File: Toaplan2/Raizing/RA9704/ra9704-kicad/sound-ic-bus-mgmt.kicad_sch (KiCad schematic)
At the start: 5 parts, among them U715 PCM_EXP1 (GAL16V8), U716 PCM_EX23 (GAL16V8), U76 A101B

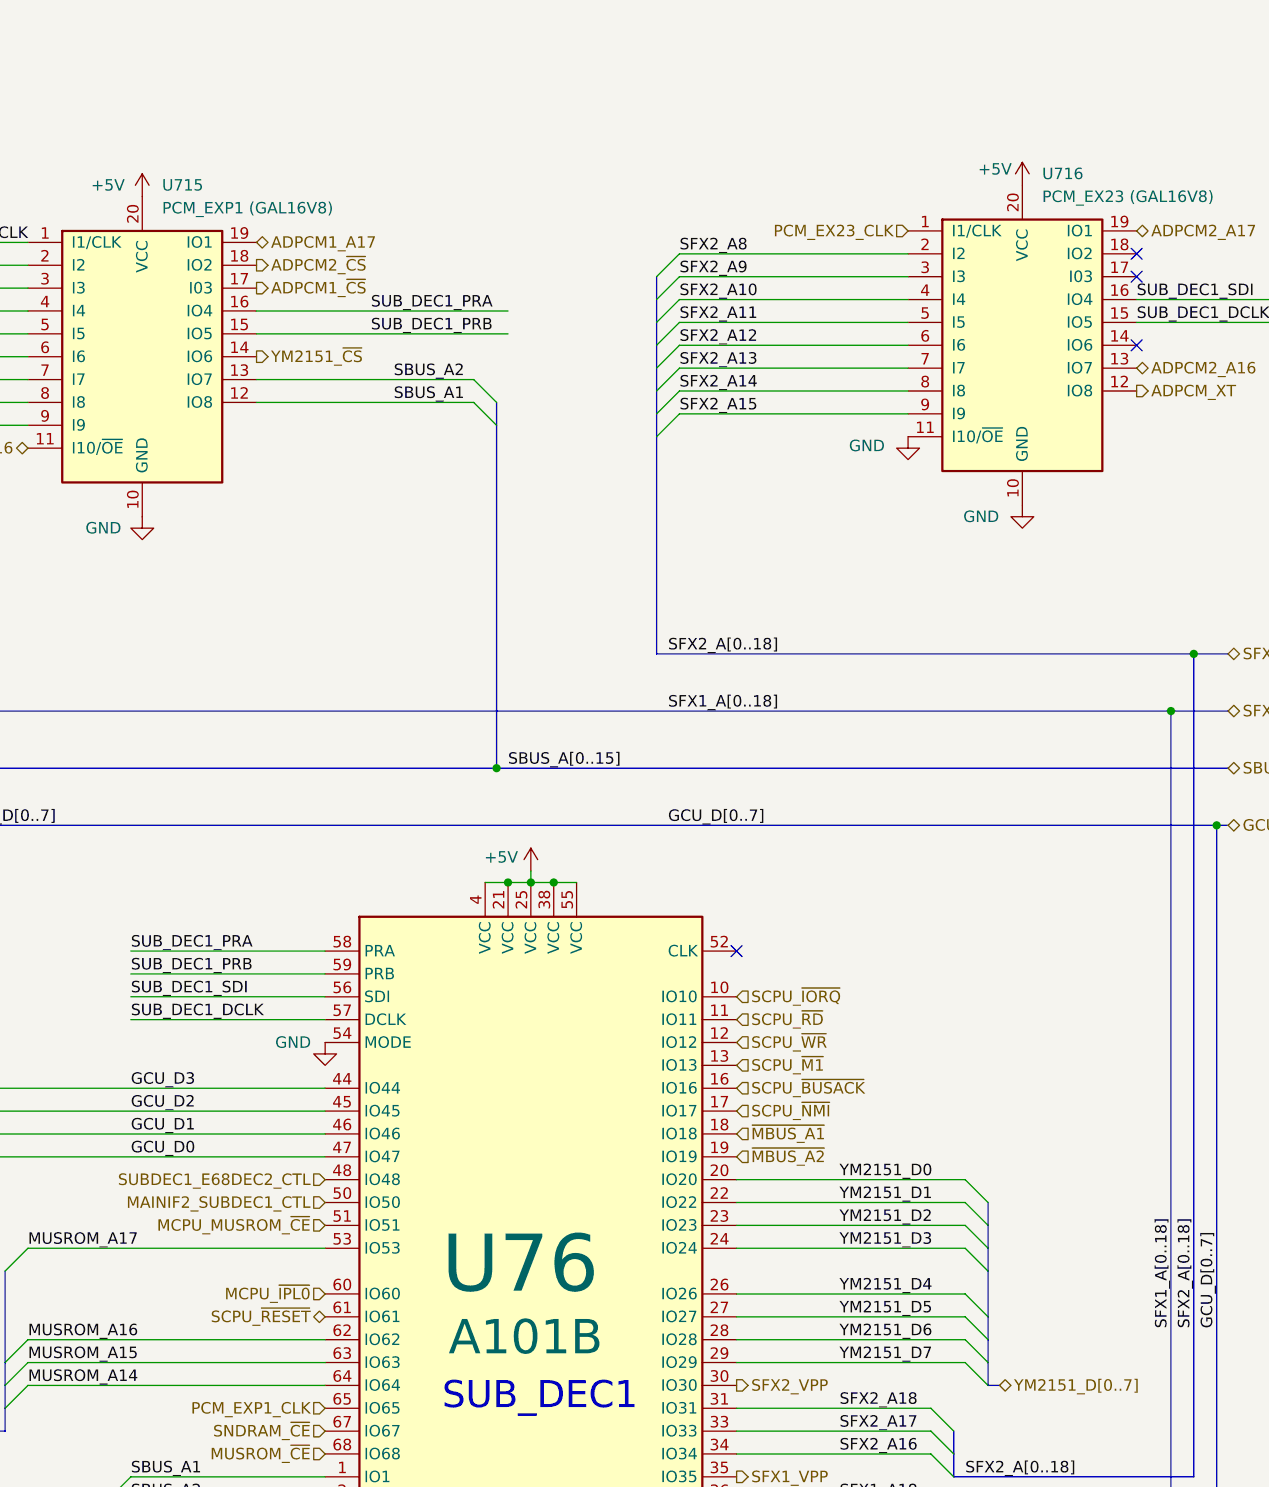
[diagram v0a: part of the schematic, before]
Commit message: fix(ra9704): Add Os as a proxy for 0s in all reference designators
RA9704 has reference designators such that each number has a preceding zero (e.g. RA076, U074, etc.). This causes a bug in KiCAD.

This is 'fixed' by using the 'O' (the letter 'Oh') character instead.

For more info, see the following issue on the KiCAD Gitlab repo

https://gitlab.com/kicad/code/kicad/-/issues/19229
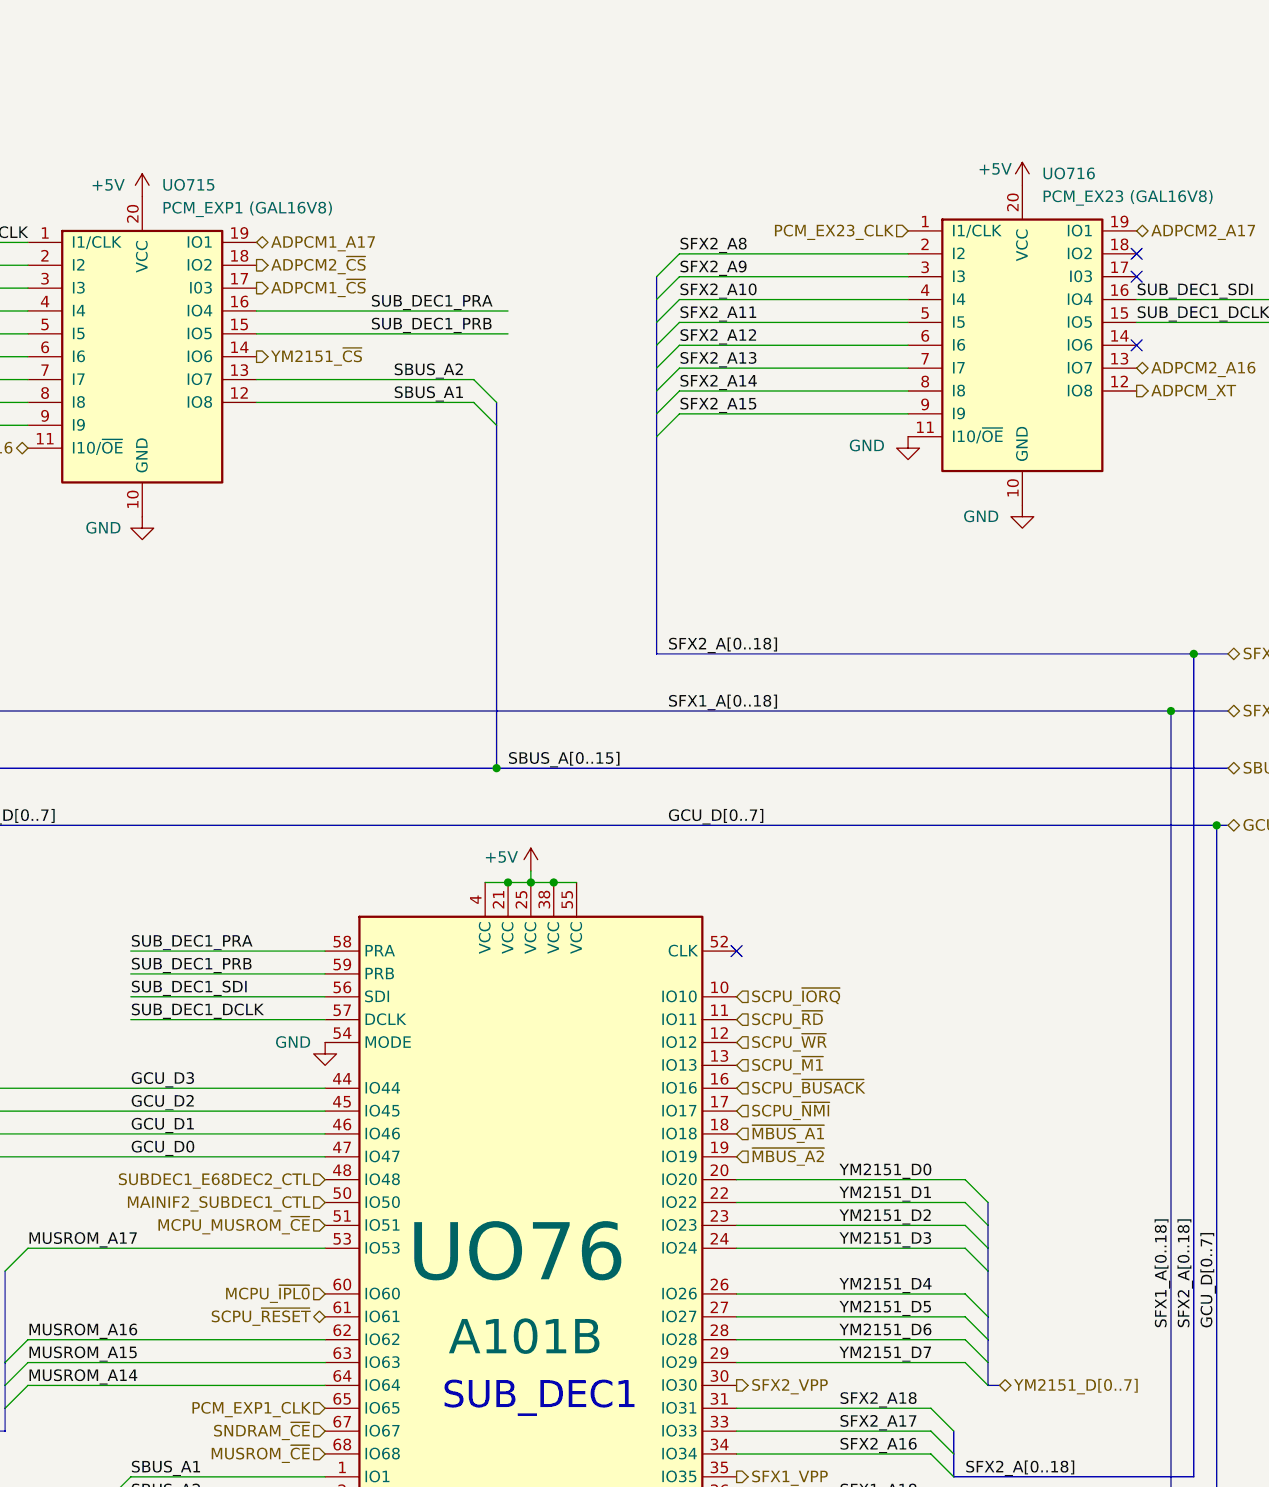
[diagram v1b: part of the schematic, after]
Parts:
- renumbered U715 to UO715, U716 to UO716, U76 to UO76
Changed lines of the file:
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@@
 		(dnp no)
 		(fields_autoplaced yes)
-		(property "Reference" "U716"
+		(property "Reference" "UO716"
 			(at 164.7541 53.34 0)
 			(effects
@@
 			(project "ra9704"
 				(path "/24d3b4cf-2360-45fc-8c40-cedc8afdf9e1/2c170486-a7cf-4da9-9098-f4bf25efe1be"
-					(reference "U716")
+					(reference "UO716")
 					(unit 1)
 				)
@@
 		(on_board yes)
 		(dnp no)
-		(property "Reference" "U76"
-			(at 98.044 174.498 0)
+		(property "Reference" "UO76"
+			(at 94.234 173.228 0)
 			(effects
 				(font
@@
 			(project "ra9704"
 				(path "/24d3b4cf-2360-45fc-8c40-cedc8afdf9e1/2c170486-a7cf-4da9-9098-f4bf25efe1be"
-					(reference "U76")
+					(reference "UO76")
 					(unit 1)
 				)
@@
 		(dnp no)
 		(fields_autoplaced yes)
-		(property "Reference" "U715"
+		(property "Reference" "UO715"
 			(at 66.9641 54.61 0)
 			(effects
@@
 			(project "ra9704"
 				(path "/24d3b4cf-2360-45fc-8c40-cedc8afdf9e1/2c170486-a7cf-4da9-9098-f4bf25efe1be"
-					(reference "U715")
+					(reference "UO715")
 					(unit 1)
 				)
